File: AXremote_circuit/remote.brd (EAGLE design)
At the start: 100 x 80 mm, 22 parts, among them Q1 16MHz, U1 AX8052F143HS

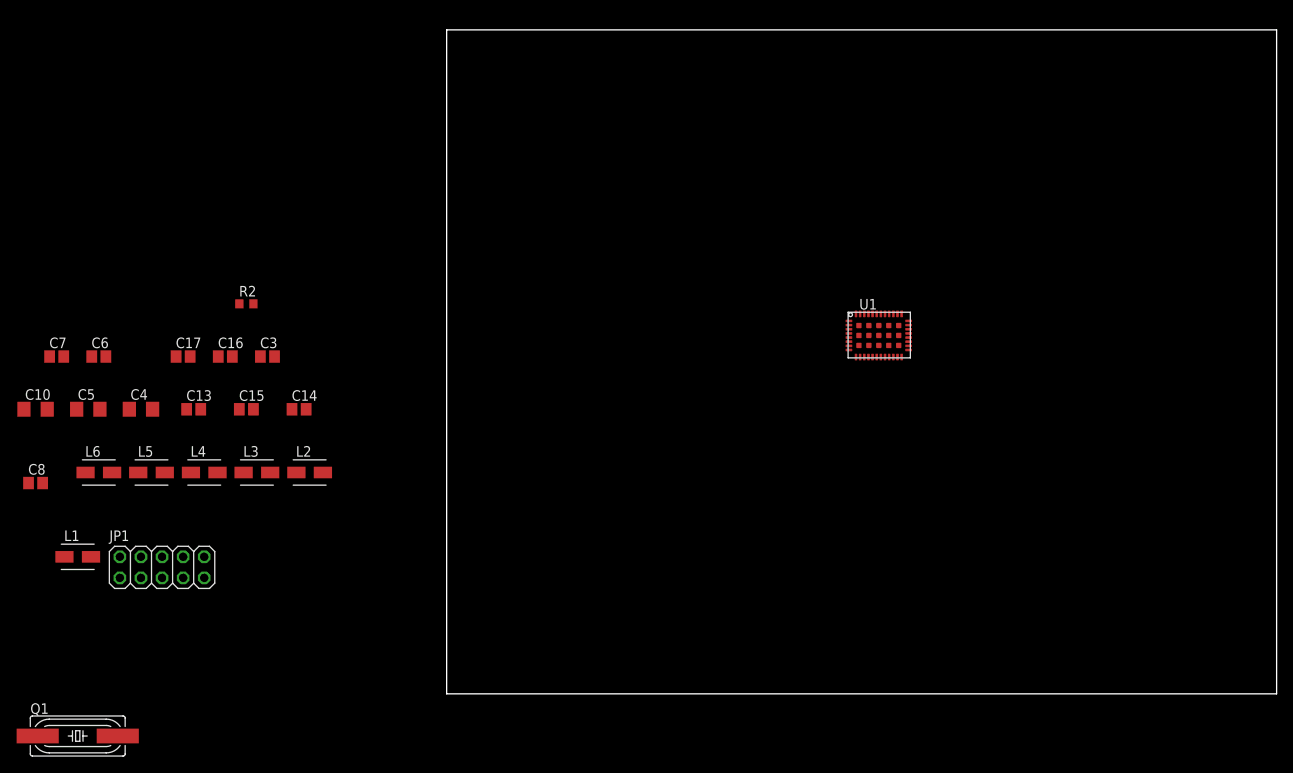
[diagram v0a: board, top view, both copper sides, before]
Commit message: Layouted board with antenna.
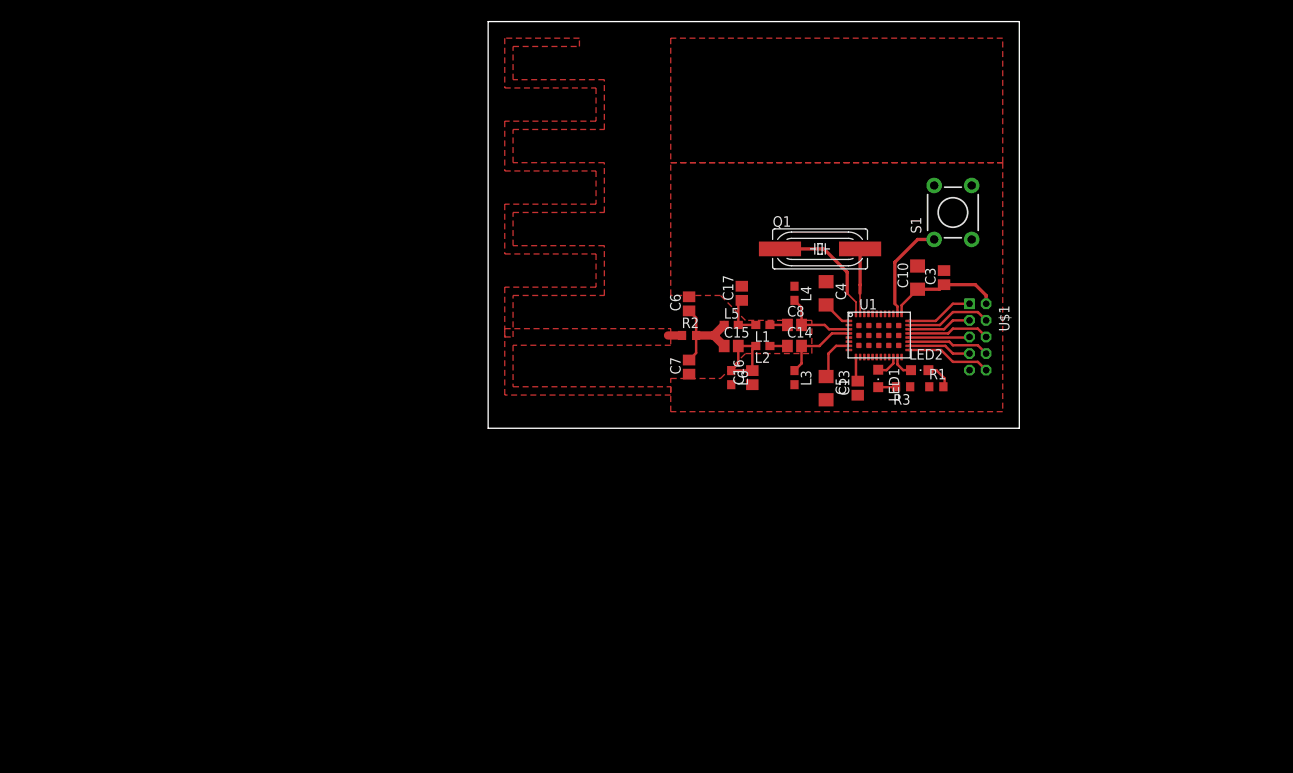
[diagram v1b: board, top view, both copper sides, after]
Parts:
- removed JP1: (no value), pinhead:2X05
- added LED1, LED2: (no value), led:CHIPLED_0805
- added R1, R3: 220, resistor:R0603
- added S1: SWITCH-MOMENTARY-2PTH, SparkFun-Electromechanical:TACTILE-PTH
- added U$1: PINHEADER5X2, sam:PINHEADER5X2AT2MM
- L1, L2, L3, L4, L5, L6: device resistor:L4035M -> resistor:C0603
- moved C10 107.4 mm to (56.7, 50.1), turned to 90 degrees
- moved Q1 107.0 mm to (45.0, 53.6)
- moved C8 93.4 mm to (41.9, 44.5)
- moved C5 88.9 mm to (45.7, 36.8), turned to 270 degrees
- moved L1 87.2 mm to (38.1, 44.5), turned to 180 degrees
- moved C4 83.7 mm to (45.7, 48.3), turned to 270 degrees
- moved C3 82.1 mm to (59.9, 50.1), turned to 90 degrees
- moved C13 80.1 mm to (49.5, 36.8), turned to 90 degrees
- moved L6 77.1 mm to (34.3, 38.1), turned to 270 degrees
- moved C7 76.2 mm to (29.2, 39.4), turned to 90 degrees
- moved L4 74.3 mm to (41.9, 48.3), turned to 270 degrees
- moved L5 72.1 mm to (34.3, 44.5)
- moved C6 71.4 mm to (29.2, 47.0), turned to 90 degrees
- moved C17 67.7 mm to (35.6, 48.3), turned to 90 degrees
- moved L3 65.8 mm to (41.9, 38.1), turned to 270 degrees
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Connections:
- new net N$16: LED2.A, U1.19
- new net N$17: LED1.A, U1.18
- new net N$19: S1.1, U1.30
- new net N$4: LED1.C, R3.2
- new net N$5: LED2.C, R1.2
- net DBG_CLK: now also U$1.P$6; no longer JP1.5
- net DBG_DATA: now also U$1.P$5; no longer JP1.6
- net DBG_EN: now also U$1.P$3; no longer JP1.4
- net GND: now also R1.1, R3.1, S1.3, U$1.P$1, U$1.P$9; no longer JP1.10, JP1.2
- net N$18: now also U$1.P$10; no longer JP1.9
- net RST_N: now also U$1.P$4; no longer JP1.3
- net RX0: now also U$1.P$8; no longer JP1.7
- net TX0: now also U$1.P$7; no longer JP1.8
- net VCC: now also U$1.P$2; no longer JP1.1
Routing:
- net N$15: track 0.00 -> 14.7 mm
- net VCC: track 0.00 -> 13.8 mm
- net N$11: track 0.00 -> 12.3 mm
- net N$19: track 0.00 -> 12.2 mm
- net N$13: track 0.00 -> 11.3 mm
- net RST_N: track 0.00 -> 10.4 mm
- net N$18: track 0.00 -> 10.3 mm
- net DBG_CLK: track 0.00 -> 9.98 mm
- net RX0: track 0.00 -> 9.92 mm
- net GND: track 0.00 -> 9.88 mm
- net N$8: track 0.00 -> 9.65 mm
- net N$7: track 0.00 -> 9.24 mm
- net N$14: track 0.00 -> 7.83 mm
- net DBG_EN: track 0.00 -> 7.77 mm
- net TX0: track 0.00 -> 7.72 mm
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- added copper zone on layer 1, net GND
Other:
- board size 100 x 80 mm -> 64 x 49 mm
- board text added: "Samuel Bryner, 2013 AX8052F143 Test rev 1"

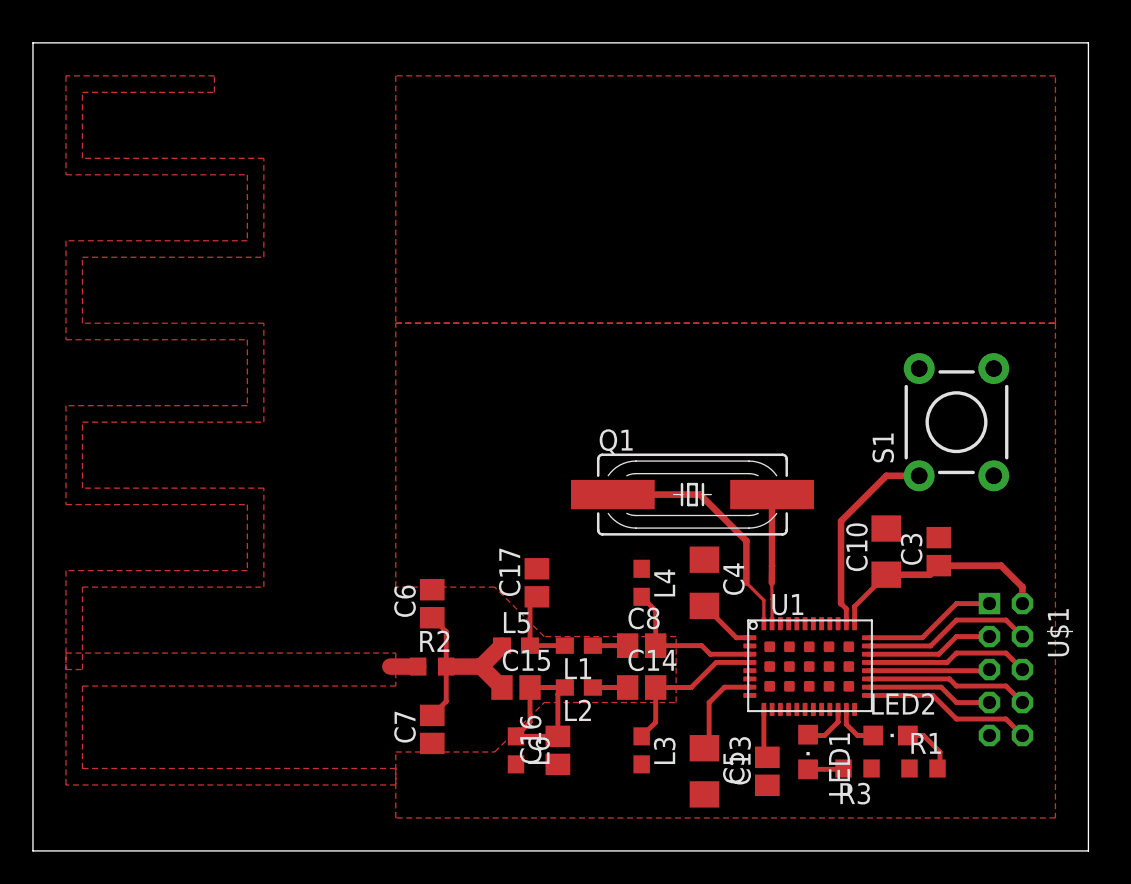
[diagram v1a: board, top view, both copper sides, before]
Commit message: Moved antenna components closer to chip, better ground connection[s].
According to Thomas' tips.
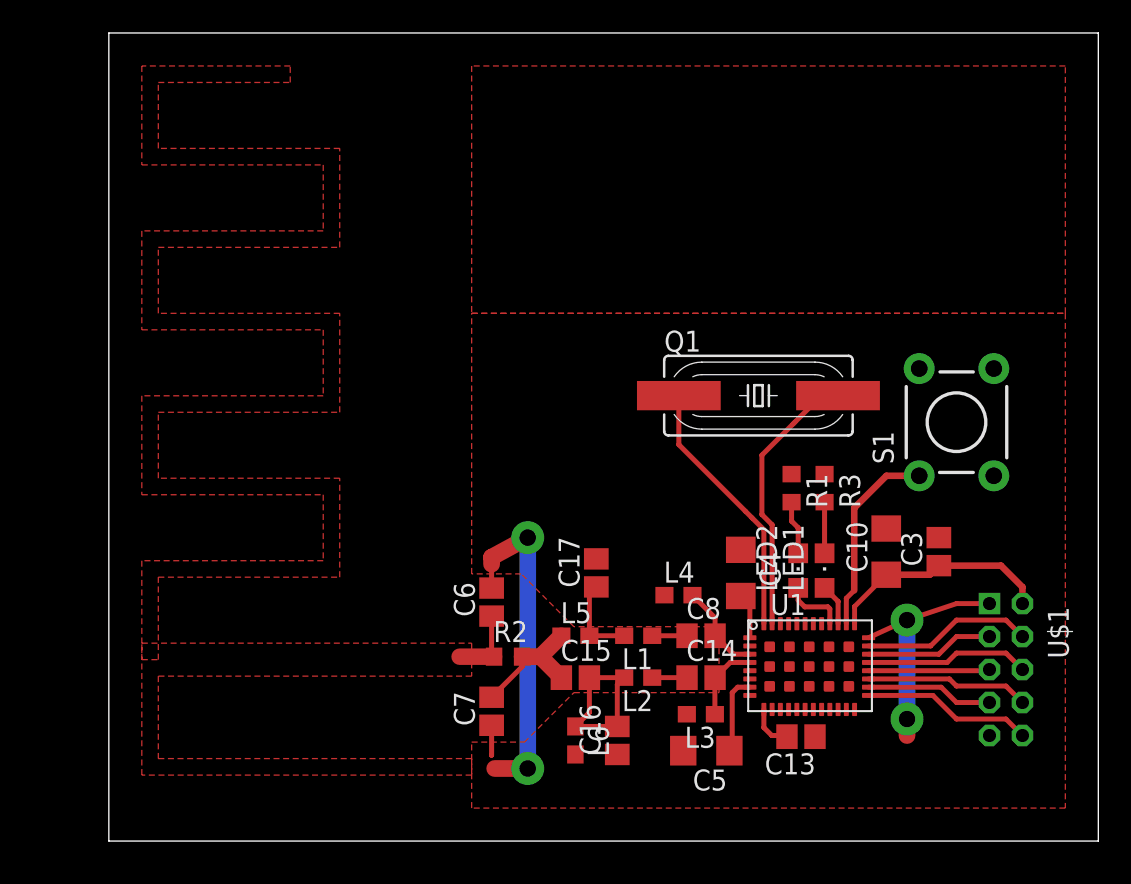
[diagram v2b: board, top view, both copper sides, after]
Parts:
- moved R1 18.8 mm to (51.0, 54.0), turned to 270 degrees
- moved R3 17.1 mm to (53.0, 54.0), turned to 270 degrees
- moved LED2 11.5 mm to (51.4, 49.0), turned to 0 degrees
- moved LED1 11.0 mm to (53.0, 49.0), turned to 0 degrees
- moved Q1 7.21 mm to (49.0, 59.6)
- moved R2 4.64 mm to (33.8, 43.8)
- moved L3 4.21 mm to (45.5, 40.3), turned to 180 degrees
- moved C7 3.76 mm to (32.8, 40.5)
- moved C14 3.65 mm to (45.5, 42.5)
- moved C15 3.65 mm to (37.9, 42.5)
- moved C16 3.65 mm to (40.4, 38.7)
- moved L2 3.65 mm to (41.7, 42.5)
- moved L6 3.65 mm to (37.9, 38.7)
- moved C8 3.65 mm to (45.5, 45.0)
- moved L1 3.65 mm to (41.7, 45.0)
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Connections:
- removed net N$17: LED1.A, U1.18
- new net N$20: C15.1, C7.2, L5.1, R2.2
- net GND: now also C6.1
- net N$11: now also LED1.A, U1.31; no longer C15.1, C6.1, C7.2, L5.1, R2.2
- net N$16: now also U1.32; no longer U1.19
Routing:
- net GND: track 9.88 -> 41.5 mm, vias 0 -> 4
- net N$11: track 12.3 -> 2.51 mm
- net N$14: track 7.83 -> 16.6 mm
- net N$20: track 0.00 -> 7.93 mm
- net N$8: track 9.65 -> 4.72 mm
- net N$7: track 9.24 -> 5.60 mm
- net N$17: track 2.94 -> 0.00 mm
- net N$15: track 14.7 -> 16.0 mm
- net N$16: track 2.81 -> 3.79 mm
- net N$6: track 5.74 -> 4.80 mm
- net N$5: track 2.17 -> 3.10 mm
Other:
- board size 64 x 49 mm -> 60 x 49 mm
- board text added: "Samuel Bryner, 2013 AX8052F143 Test rev 1b"
- board text removed: "Samuel Bryner, 2013 AX8052F143 Test rev 1"
